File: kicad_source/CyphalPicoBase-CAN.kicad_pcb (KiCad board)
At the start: 2 copper layers, 52 x 36 mm, 62 parts, among them CN1 RASPBERRYPI_PICO, CN12 S3B-PH-SM4-TB, CN2 SM04B-SRSS-TB, CN3 SM04B-SRSS-TB, CN4 SM04B-GHS-TB, CN5 SM04B-GHS-TB, CN7 DNI, CN8 DNI, SW1 PTS636 SM43 SMTR LFS, U3 M24C64-RMN6TP, U8 MCP2515T-I/SO, U9 SN65HVD230, Y1 X322516MLB4SI

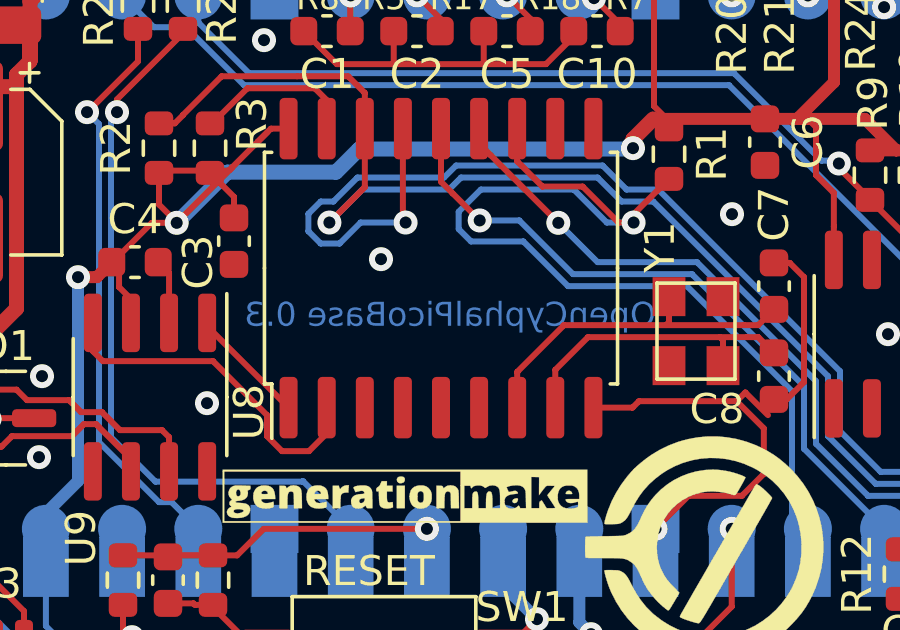
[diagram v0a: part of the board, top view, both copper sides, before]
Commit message: updated labels in schematic, updated pdf and images
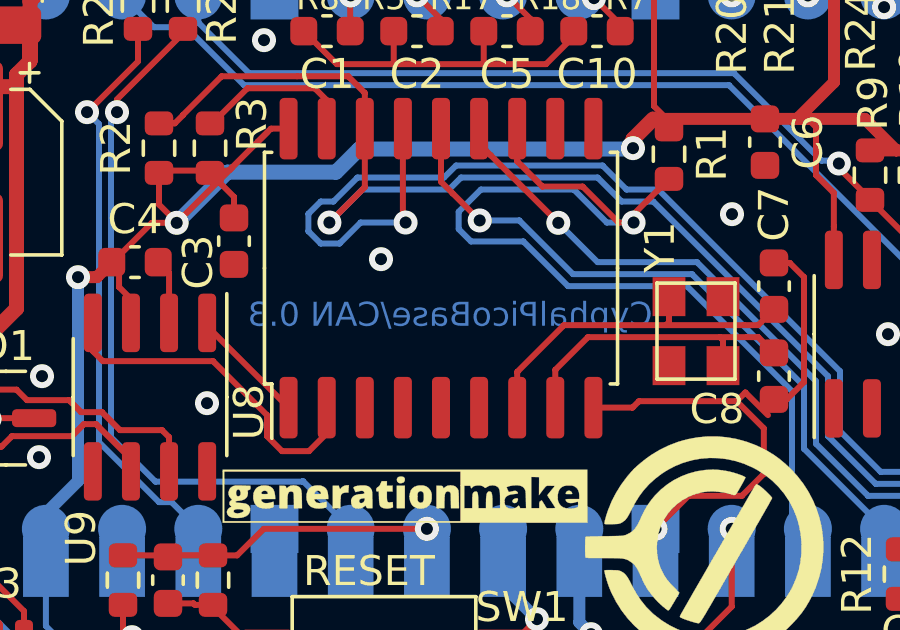
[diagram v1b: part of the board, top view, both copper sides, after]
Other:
- board text added: "CyphalPicoBase/CAN 0.3"
- board text added: "find data and documentation at https://github.com/generationmake/CyphalPicoBase-CAN"
- board text removed: "OpenCyphalPicoBase 0.3"
- board text removed: "find data and documentation at https://github.com/generationmake/OpenCyphalPicoBase"
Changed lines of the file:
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@@
   (paper "A4")
   (title_block
-    (title "OpenCyphalPicoBase")
-    (date "2023-08-08")
+    (title "CyphalPicoBase/CAN")
+    (date "2023-09-21")
     (rev "0.3")
     (company "generationmake")
@@
     (effects (font (size 1.5 1.5) (thickness 0.375)))
   )
-  (gr_text "OpenCyphalPicoBase 0.3" (at 89.5 93.75) (layer "B.Cu")
+  (gr_text "CyphalPicoBase/CAN 0.3" (at 89.5 93.75) (layer "B.Cu")
     (effects (font (size 0.8 0.8) (thickness 0.2)) (justify mirror))
   )
@@
     (effects (font (size 0.6 0.6) (thickness 0.15)) (justify right mirror))
   )
-  (gr_text "find data and documentation at\nhttps://github.com/generationmake/OpenCyphalPicoBase" (at 96.3 105.5) (layer "B.SilkS")
+  (gr_text "find data and documentation at\nhttps://github.com/generationmake/CyphalPicoBase-CAN" (at 96.8 105.8) (layer "B.SilkS")
     (effects (font (size 0.6 0.6) (thickness 0.15)) (justify left mirror))
   )
